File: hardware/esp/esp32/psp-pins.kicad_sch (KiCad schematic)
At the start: 52 parts, among them U1 MCP23008-E/ML, U4 MCP23008-E/ML, U5 MCP42010T-I/SL

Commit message: wip
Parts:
- removed Center2: 5034801000, JLCPCB_footprint:FPC-SMD_5034801000, symbol JLCPCB_schematic:5034801000
- removed R5, R6: 0805W8F4701T5E, JLCPCB_footprint:R0805, symbol JLCPCB_schematic:0805W8F4701T5E
- removed U1, U4: MCP23008-E/ML, JLCPCB_footprint:QFN-20_L4.0-W4.0-P0.50-BL-EP2.7, symbol JLCPCB_schematic:MCP23008-E/ML
- added R6: 0402WGF1002TCE, JLCPCB_footprint:R0402, symbol JLCPCB_schematic:0402WGF1002TCE
- added TP11, TP37, TP38, TP39: TestPoint, TestPoint:TestPoint_Pad_D1.0mm, symbol Connector:TestPoint
- added U6: TS5A23157DGSR, JLCPCB_footprint:MSOP-10_L3.0-W3.0-P0.50-LS5.0-BL, symbol JLCPCB_schematic:TS5A23157DGSR
- added U7: IPFP051A30472R5, JLCPCB_footprint:FPC-SMD_4P-P0.50_C9900013912, symbol JLCPCB_schematic:IPFP051A30472R5
- TP7, TP8: footprint TestPoint:TestPoint_Pad_1.5x1.5mm -> TestPoint:TestPoint_Pad_D1.0mm
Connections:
- net +V: now also TP8.1, U7.2
- net GND: now also R6.2, U6.3 (GND), U7.4
- net at TP7.1: now also U6.8 (V+)
- net Circle renamed circle
- net Cross renamed cross
- net Display renamed display
- net Down renamed down
- net Home renamed home
- net Left renamed left
- net R1 renamed r1
- net Right renamed right
- net Sound renamed sound
- net Square renamed square
- net Triangle renamed triangle
- net Up renamed up
- net VolDown renamed voldown
- net VolUp renamed volup
- removed net X_1: Analog1.2, Analog1.8, TP1.1, TP4.1, U5.9 (PW0)
- removed net Y_1: Analog1.1, Analog1.10, TP2.1, TP3.1, U5.6 (PW1)
- new net Analog_toggle: U6.1 (IN_1), U6.5 (IN_2)
- new net Analog_x: Analog1.8, TP11.1, TP38.1, U6.9 (NC_1), U7.1
- new net Annalog_y: Analog1.10, TP37.1, TP39.1, U6.7 (NC_2), U7.3
- new net PSP_x: Analog1.2, U6.10 (COM_1)
- new net PSP_y: Analog1.1, U6.6 (COM2)
- new net digi-X: U5.9 (PW0), U6.2 (NO_1)
- new net digi-y: U5.6 (PW1), U6.4 (NO_2)
- no-connect marks 18 -> 10
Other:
- note removed: "16 bank expanders not available at JLCPCB so use two 8 bank instead"
- note removed: "Address 0x20"
- note removed: "Address 0x21"
- note removed: "Annoyingly io expanders font have enough for all psp pins. Start go stright to ESP."
- note removed: "I think only one set of I2C pull up resistors needed even though there are two devices"
- note removed: "IO expanders"
- moved on the sheet: Analog1, Center1, D1, D10, D11, D12, D20, D24, D25, D26, D27, D28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

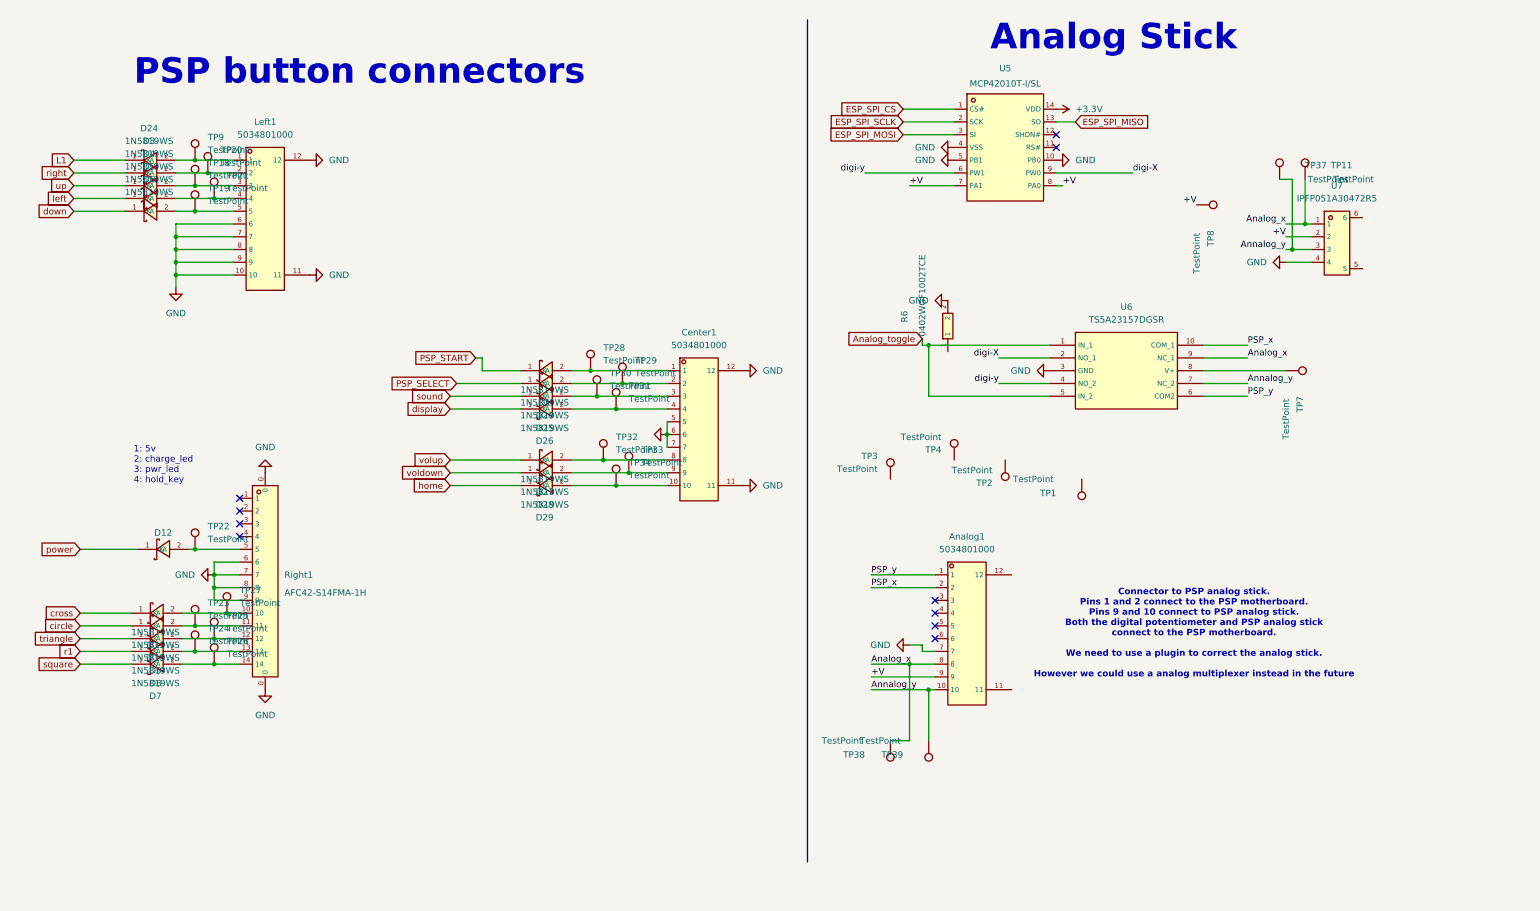
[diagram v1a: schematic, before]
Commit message: Added hardware 0.2 - Added right FPC
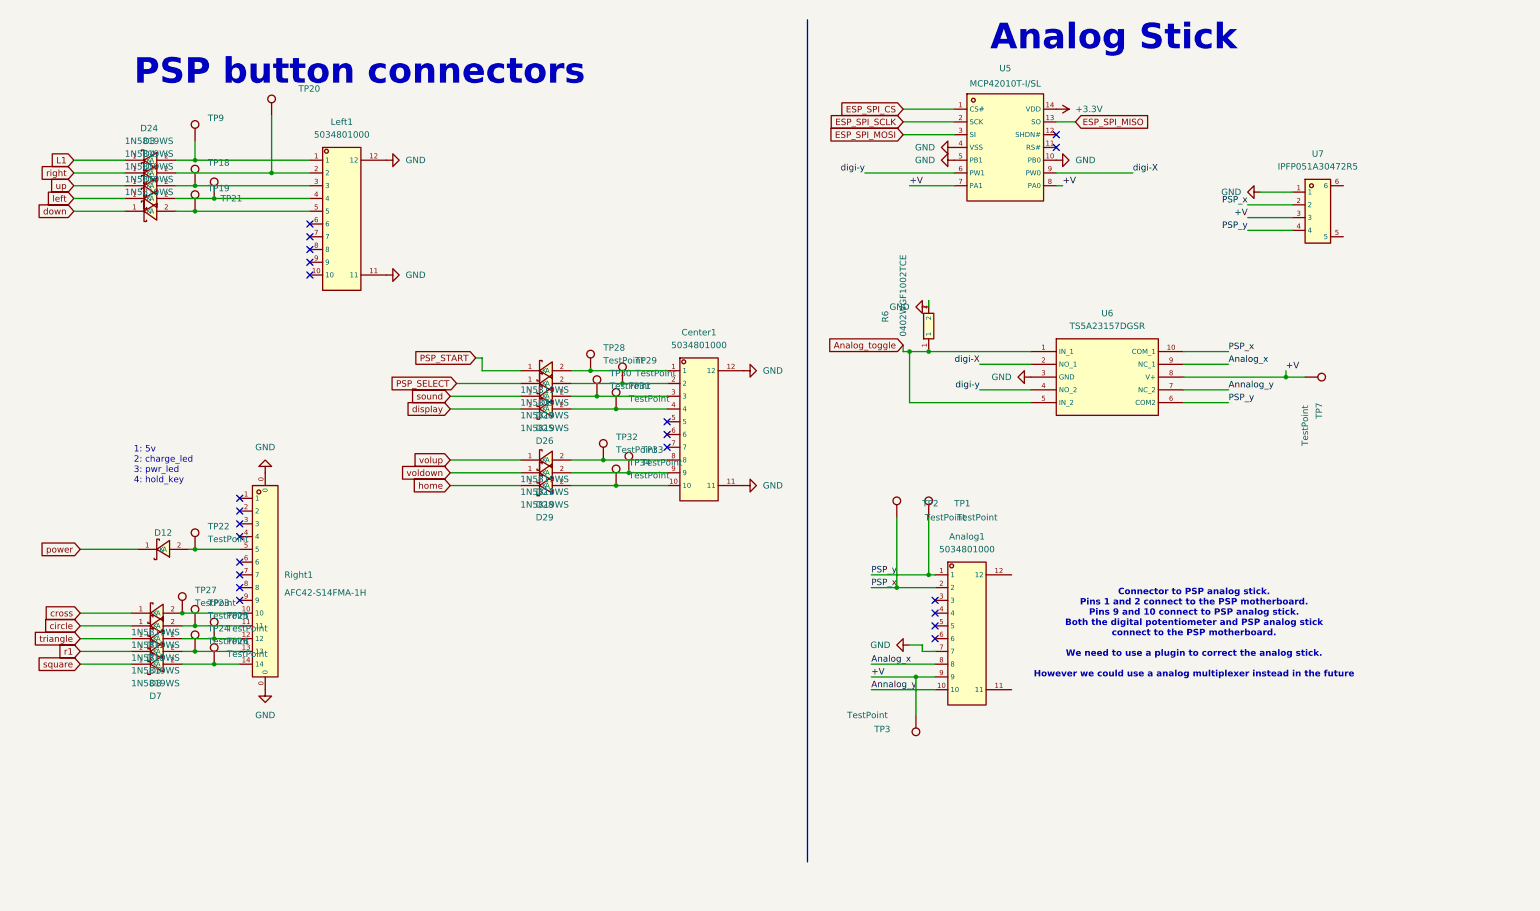
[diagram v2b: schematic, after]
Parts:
- removed TP11, TP37, TP38, TP39, TP8: TestPoint, TestPoint:TestPoint_Pad_D1.0mm, symbol Connector:TestPoint
- removed TP4: TestPoint, TestPoint:TestPoint_Pad_1.5x1.5mm, symbol Connector:TestPoint
- TP1, TP2, TP3: footprint TestPoint:TestPoint_Pad_1.5x1.5mm -> TestPoint:TestPoint_Pad_D1.0mm
- TP18, TP19, TP20, TP21, TP22, TP23, TP24, TP25, TP26, TP27, TP28, TP29, TP30, TP31, TP32, TP33, TP34, TP9: footprint TestPoint:TestPoint_Pad_1.0x1.0mm -> TestPoint:TestPoint_Pad_D1.0mm
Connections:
- net +V: now also TP3.1, TP7.1, U6.8 (V+), U7.3; no longer U7.2
- net Analog_toggle: now also R6.1
- net Analog_x: no longer U7.1
- net Annalog_y: no longer U7.3
- net GND: now also U7.1; no longer Center1.5, Center1.6, Center1.7, Left1.10, Left1.6, Left1.7, Left1.8, Left1.9, Right1.6, Right1.7, Right1.8, Right1.9, U7.4
- net PSP_x: now also TP2.1, U7.2
- net PSP_y: now also TP1.1, U7.4
- no-connect marks 10 -> 22
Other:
- moved on the sheet: Left1, R6, TP20, TP27, TP7, TP9, U6

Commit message: stuff
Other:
- note added: "Connector to PSP analog stick. Pins 1 and 2 connect to the PSP motherboard. Pins 9 and 10 connect to PSP analog stick. So the analog sticks (real and digi pot) are not connected in parallel a analog mux is used to toggle between one or the other"
- note added: "I use diodes everywhere to try and protect PSP incase i send a pin high. No idea if itll work or even needed."
- note removed: "Connector to PSP analog stick. Pins 1 and 2 connect to the PSP motherboard. Pins 9 and 10 connect to PSP analog stick. Both the digital potentiometer and PSP analog stick connect to the PSP motherboard. We need to use a plugin to correct the analog stick. However we could use a analog multiplexer instead in the future"
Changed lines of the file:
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@@
+		)
+	)
+	(text "I use diodes everywhere to try and protect PSP\nincase i send a pin high. No idea if itll work or even needed."
+		(exclude_from_sim no)
+		(at 125.222 39.624 0)
+		(effects
+			(font
+				(size 1.27 1.27)
+			)
 		)
 	)
@@
 		)
 	)
-	(text "Connector to PSP analog stick. \nPins 1 and 2 connect to the PSP motherboard. \nPins 9 and 10 connect to PSP analog stick.\nBoth the digital potentiometer and PSP analog stick\nconnect to the PSP motherboard.\n\nWe need to use a plugin to correct the analog stick.\n\nHowever we could use a analog multiplexer instead in the future"
+	(text "Connector to PSP analog stick. \nPins 1 and 2 connect to the PSP motherboard. \nPins 9 and 10 connect to PSP analog stick.\n\nSo the analog sticks (real and digi pot) are\nnot connected in parallel a analog mux is used\nto toggle between one or the other"
 		(exclude_from_sim no)
 		(at 244.602 139.954 0)
